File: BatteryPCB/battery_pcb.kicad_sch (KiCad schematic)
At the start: 0 parts

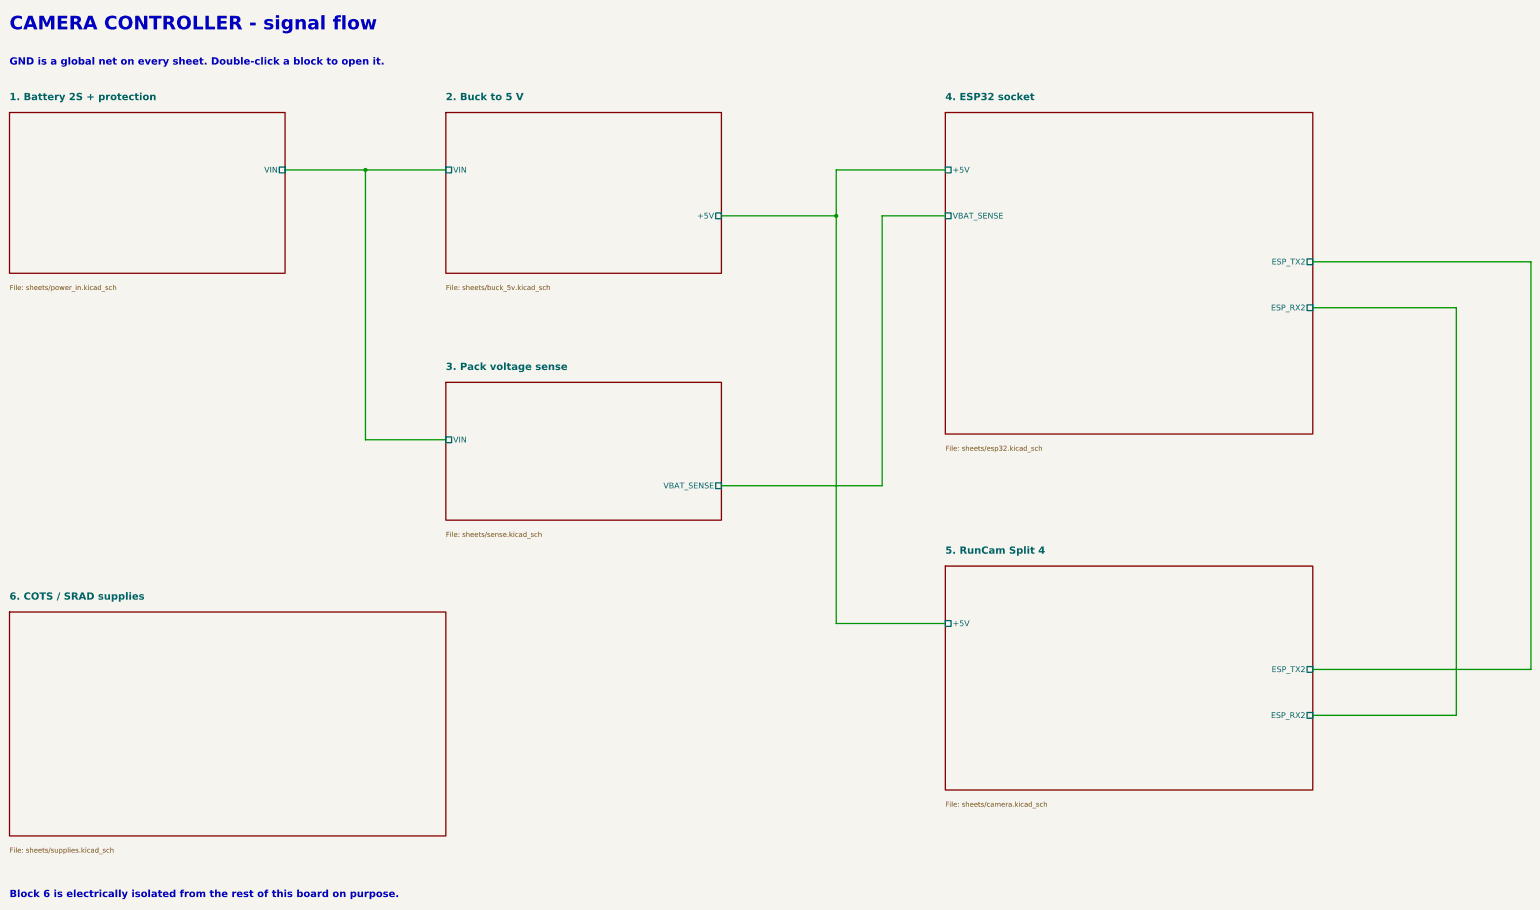
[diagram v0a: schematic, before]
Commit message: Battery PCB schematic: ESP32, camera and pack-sense sheets merged; C9/C10 on the buck output
Schematic only: sheets 3-5 become one wired sheet (3. ESP32 + camera), C9/C10 move
to the buck sheet's +5V output, supplies renumbered 6 -> 4. Every connection,
part, value and footprint is unchanged; the board only gets the new sheet paths
and net-name prefixes (tools/sync_from_sch.py). Gerbers and drills are
geometrically identical to v22. DRC 0 with schematic parity.

Co-Authored-By: Claude Opus 5.5 <noreply@anthropic.com>
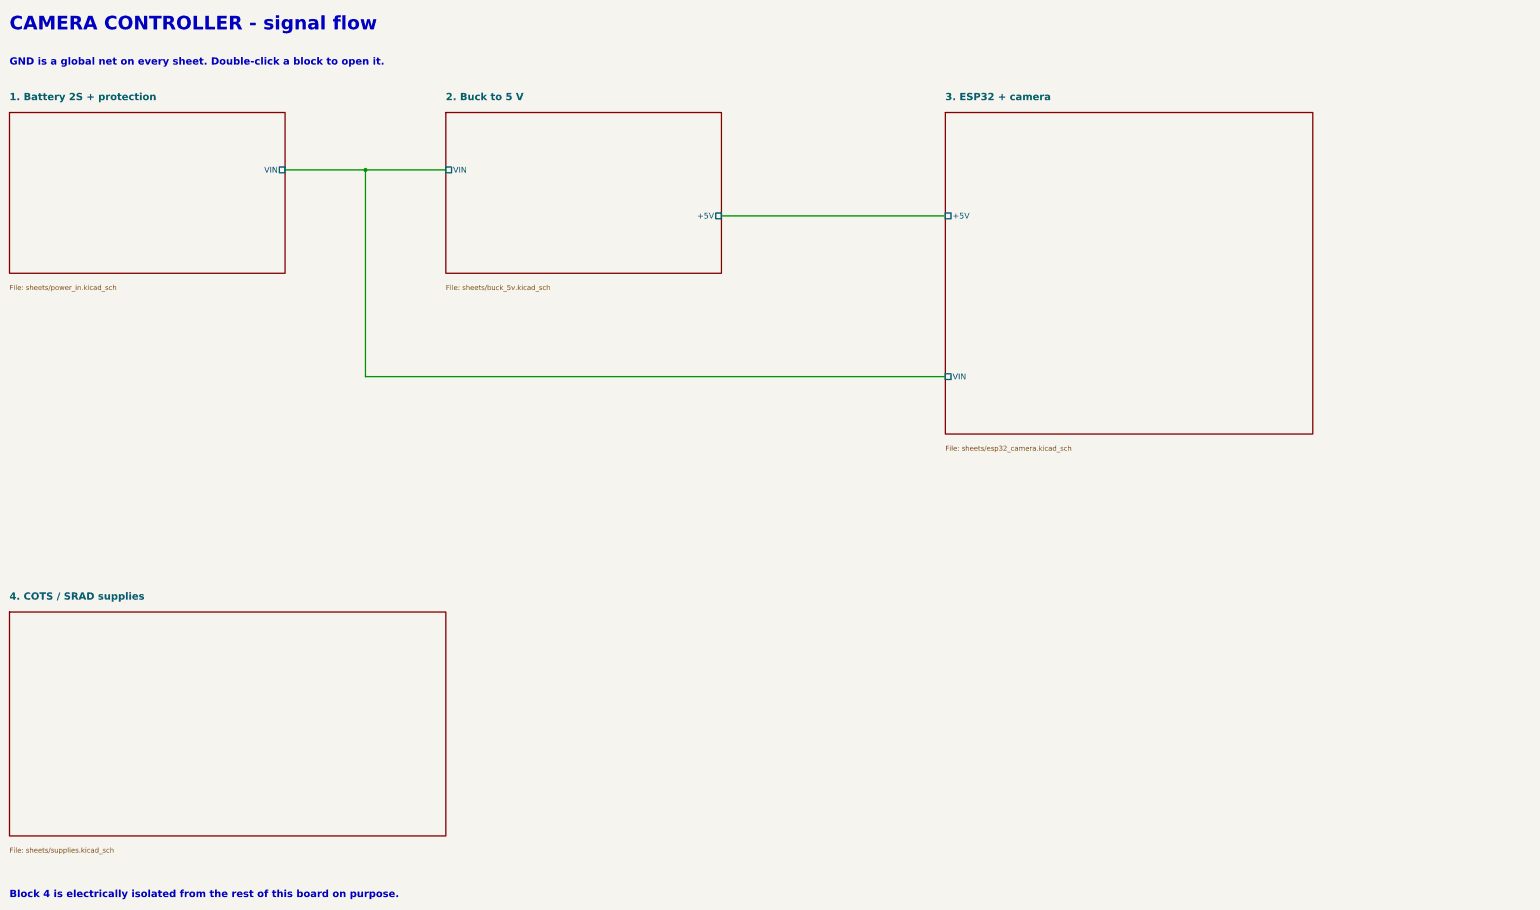
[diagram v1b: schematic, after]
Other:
- sheet 4. ESP32 socket renamed 3. ESP32 + camera
- sheet 6. COTS / SRAD supplies renamed 4. COTS / SRAD supplies
- removed sheet 3. Pack voltage sense
- removed sheet 5. RunCam Split 4
- sheet 3. ESP32 + camera: file sheets/esp32.kicad_sch -> sheets/esp32_camera.kicad_sch
- sheet 3. ESP32 + camera ports: added VIN; removed ESP_RX2, ESP_TX2, VBAT_SENSE
- note added: "Block 4 is electrically isolated from the rest of this board on purpose."
- note removed: "Block 6 is electrically isolated from the rest of this board on purpose."

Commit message: Battery PCB: schematic sheets re-saved after cleanup; board net names re-escaped
Same design as 428171c: identical netlist (42 parts, 55 nets, same pins,
values, footprints and MPNs) and identical board geometry. The board only
changes the sheet-name escaping inside net names ("COTS / SRAD" ->
"COTS {slash} SRAD").

Checks on this commit: ERC 0 errors; strict DRC 0 violations, 0 unconnected,
0 schematic parity issues (also with zones refilled); verify_A.py ALL PASS.
New ERC warnings: 16 endpoint_off_grid on the root and COTS/SRAD sheets
(half-grid wire ends and J6 pin 1); connectivity is unaffected.

Co-Authored-By: Claude Opus 5.5 <noreply@anthropic.com>
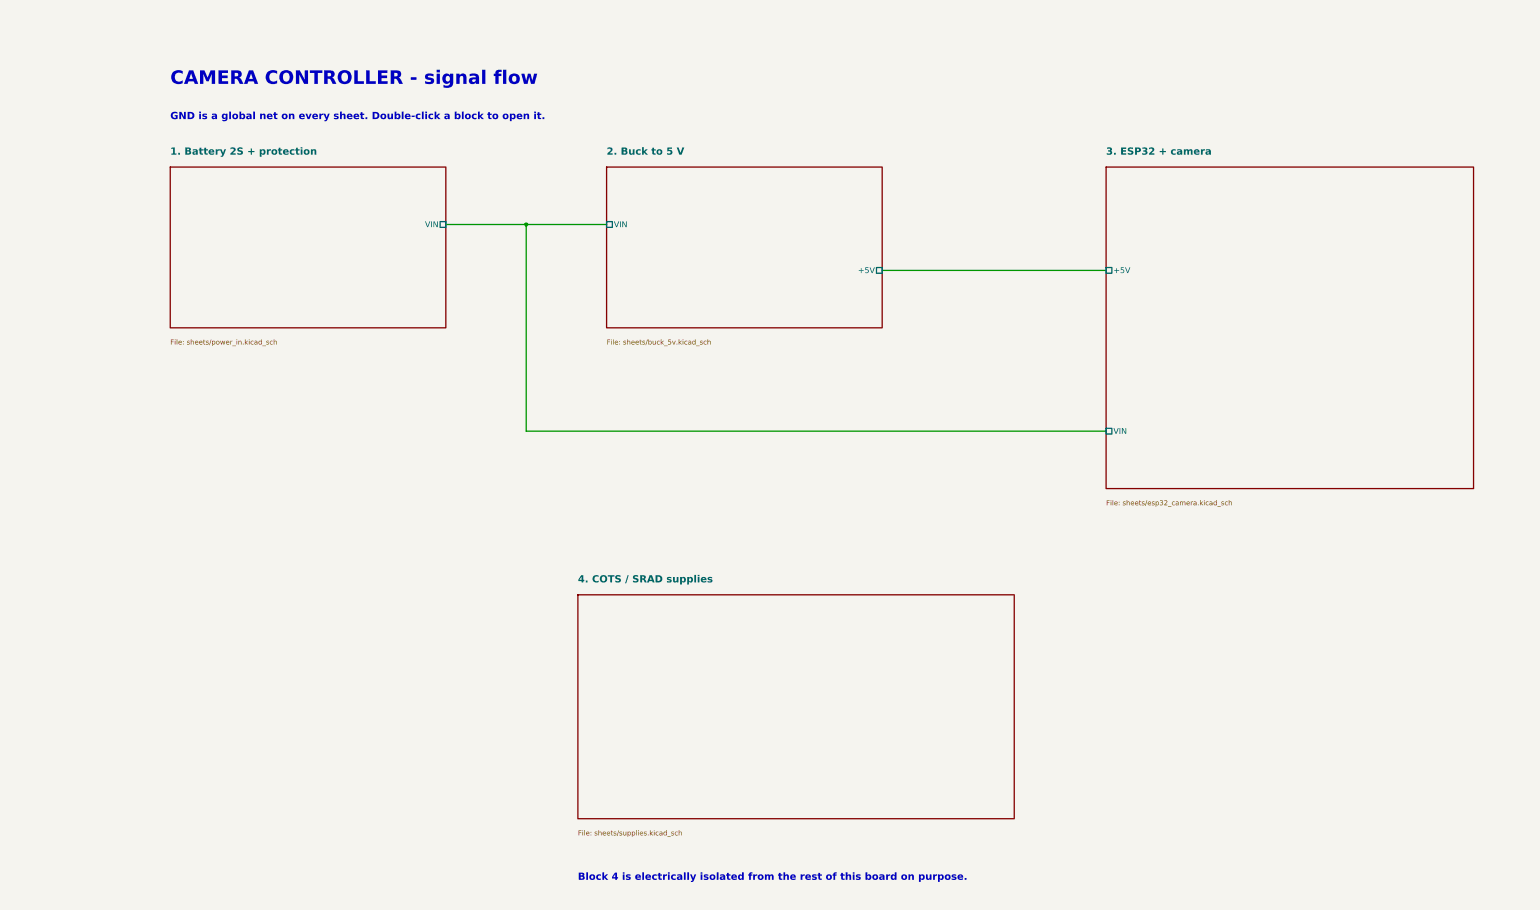
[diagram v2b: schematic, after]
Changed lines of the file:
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@@
 	(text "CAMERA CONTROLLER - signal flow"
 		(exclude_from_sim no)
-		(at 25.4 24.13 0)
+		(at 60.96 36.195 0)
 		(effects
 			(font
@@
 	(text "GND is a global net on every sheet. Double-click a block to open it."
 		(exclude_from_sim no)
-		(at 25.4 31.75 0)
+		(at 60.96 43.815 0)
 		(effects
 			(font
@@
 	(text "Block 4 is electrically isolated from the rest of this board on purpose."
 		(exclude_from_sim no)
-		(at 25.4 215.9 0)
+		(at 151.13 212.09 0)
 		(effects
 			(font
@@
 		)
 	)
-	(wire
-		(pts
-			(xy 86.36 54.61)
-			(xy 104.14 54.61)
-		)
-		(stroke
-			(width 0)
-			(type default)
-		)
-	)
-	(wire
-		(pts
-			(xy 104.14 54.61)
-			(xy 121.92 54.61)
-		)
-		(stroke
-			(width 0)
-			(type default)
-		)
-	)
 	(junction
-		(at 104.14 54.61)
+		(at 139.7 66.675)
 		(diameter 0)
 		(color 0 0 0 0)
@@
 	(wire
 		(pts
-			(xy 104.14 54.61)
-			(xy 104.14 100.33)
-		)
-		(stroke
-			(width 0)
-			(type default)
-		)
-	)
-	(wire
-		(pts
-			(xy 104.14 100.33)
-			(xy 232.41 100.33)
-		)
-		(stroke
-			(width 0)
-			(type default)
-		)
-	)
-	(wire
-		(pts
-			(xy 182.88 64.77)
-			(xy 232.41 64.77)
-		)
-		(stroke
-			(width 0)
-			(type default)
-		)
-	)
-	(sheet
-		(at 121.92 41.91)
+			(xy 121.92 66.675) (xy 139.7 66.675)
+		)
+		(stroke
+			(width 0)
+			(type default)
+		)
+	)
+	(wire
+		(pts
+			(xy 139.7 112.395) (xy 267.97 112.395)
+		)
+		(stroke
+			(width 0)
+			(type default)
+		)
+	)
+	(wire
+		(pts
+			(xy 139.7 66.675) (xy 157.48 66.675)
+		)
+		(stroke
+			(width 0)
+			(type default)
+		)
+	)
+	(wire
+		(pts
+			(xy 139.7 66.675) (xy 139.7 112.395)
+		)
+		(stroke
+			(width 0)
+			(type default)
+		)
+	)
+	(wire
+		(pts
+			(xy 218.44 76.835) (xy 267.97 76.835)
+		)
+		(stroke
+			(width 0)
+			(type default)
+		)
+	)
+	(sheet
+		(at 157.48 53.975)
 		(size 60.96 35.56)
 		(exclude_from_sim no)
@@
 		)
 		(property "Sheetname" "2. Buck to 5 V"
-			(at 121.92 39.37 0)
+			(at 157.48 51.435 0)
 			(show_name no)
 			(do_not_autoplace no)
@@
 		)
 		(property "Sheetfile" "sheets/buck_5v.kicad_sch"
-			(at 121.92 80.01 0)
+			(at 157.48 92.075 0)
 			(show_name no)
 			(do_not_autoplace no)
@@
 		)
 		(pin "VIN" passive
-			(at 121.92 54.61 180)
+			(at 157.48 66.675 180)
 			(effects
 				(font
@@
 		)
 		(pin "+5V" passive
-			(at 182.88 64.77 0)
+			(at 218.44 76.835 0)
 			(effects
 				(font
@@
 	)
 	(sheet
-		(at 232.41 41.91)
+		(at 267.97 53.975)
 		(size 81.28 71.12)
 		(exclude_from_sim no)
@@
 		)
 		(property "Sheetname" "3. ESP32 + camera"
-			(at 232.41 39.37 0)
+			(at 267.97 51.435 0)
 			(show_name no)
 			(do_not_autoplace no)
@@
 		)
 		(property "Sheetfile" "sheets/esp32_camera.kicad_sch"
-			(at 232.41 115.57 0)
+			(at 267.97 127.635 0)
 			(show_name no)
 			(do_not_autoplace no)
@@
 		)
 		(pin "+5V" passive
-			(at 232.41 64.77 180)
+			(at 267.97 76.835 180)
 			(effects
 				(font
@@
 		)
 		(pin "VIN" passive
-			(at 232.41 100.33 180)
+			(at 267.97 112.395 180)
 			(effects
 				(font
@@
 	)
 	(sheet
-		(at 25.4 41.91)
+		(at 60.96 53.975)
 		(size 60.96 35.56)
 		(exclude_from_sim no)
@@
 		)
 		(property "Sheetname" "1. Battery 2S + protection"
-			(at 25.4 39.37 0)
+			(at 60.96 51.435 0)
 			(show_name no)
 			(do_not_autoplace no)
@@
 		)
 		(property "Sheetfile" "sheets/power_in.kicad_sch"
-			(at 25.4 80.01 0)
+			(at 60.96 92.075 0)
 			(show_name no)
 			(do_not_autoplace no)
@@
 		)
 		(pin "VIN" passive
-			(at 86.36 54.61 0)
+			(at 121.92 66.675 0)
 			(effects
 				(font
@@
 	)
 	(sheet
-		(at 25.4 152.4)
+		(at 151.13 148.59)
 		(size 96.52 49.53)
 		(exclude_from_sim no)
@@
 		)
 		(property "Sheetname" "4. COTS / SRAD supplies"
-			(at 25.4 149.86 0)
+			(at 151.13 146.05 0)
 			(show_name no)
 			(do_not_autoplace no)
@@
 		)
 		(property "Sheetfile" "sheets/supplies.kicad_sch"
-			(at 25.4 204.47 0)
-			(show_name no)
-			(do_not_autoplace no)
+			(at 151.13 200.66 0)
+			(show_name no)
+			(do_not_autoplace no)
